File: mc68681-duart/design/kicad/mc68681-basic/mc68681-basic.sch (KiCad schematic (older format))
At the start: 29 parts, among them IC1 68681, IC2 74HCT245, IC3 74HCT245, IC5 74126, IC6 IC6_DECO.PLD, IC7 IC7_UART_.PLD, J1 Conn_02x32_Odd_Even, J2 EXTBUS, J3 UART_A, J4 UART_B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

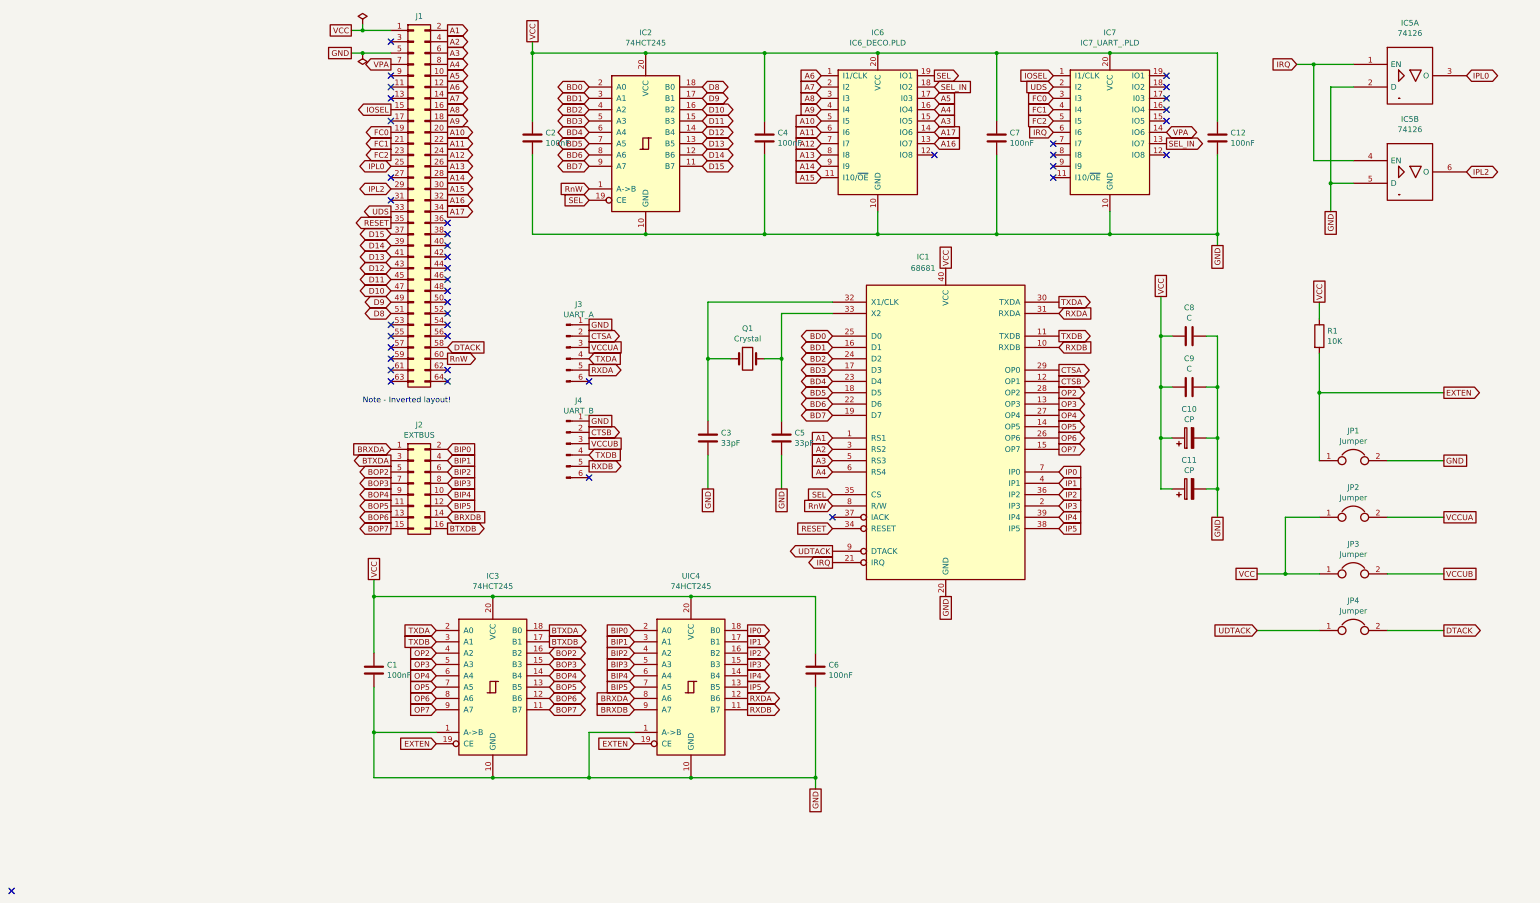
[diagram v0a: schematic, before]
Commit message: r0 layout, PLD changes for same
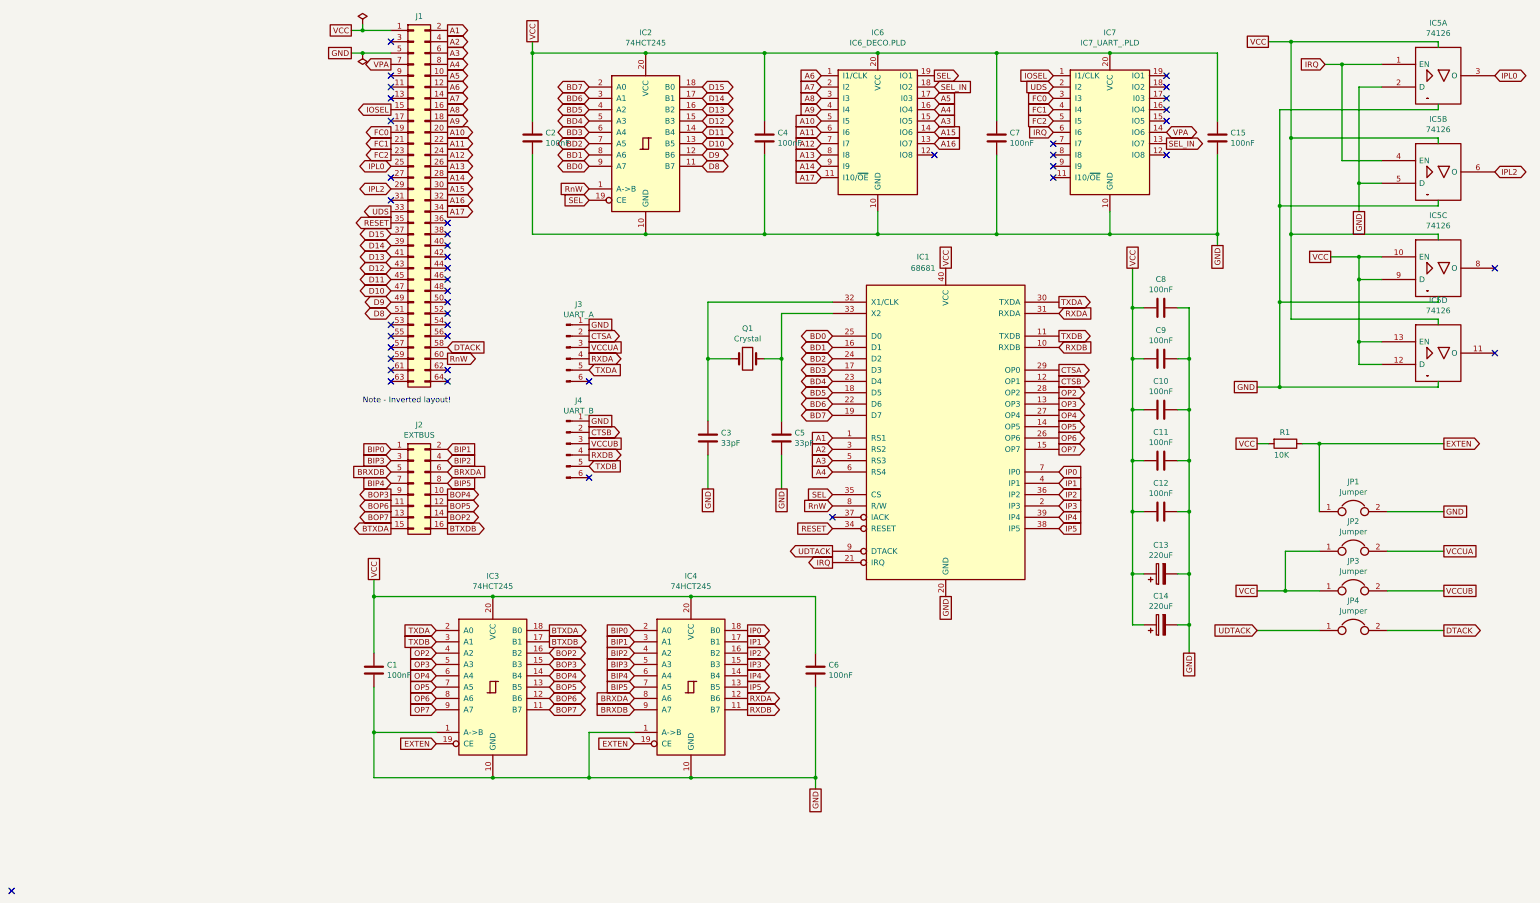
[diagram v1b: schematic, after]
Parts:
- added C10, C11, C12: 100nF, rosco_m68k:C2.5-3, symbol Device:C
- added unit 3 of IC5
- added unit 4 of IC5
- C1, C2, C3, C4, C5, C6, C7: footprint (none) -> rosco_m68k:C2.5-3
- C13: renamed from C10; value CP -> 220uF; footprint (none) -> Capacitor_THT:CP_Radial_D6.3mm_P2.50mm
- C14: renamed from C11; value CP -> 220uF; footprint (none) -> Capacitor_THT:CP_Radial_D6.3mm_P2.50mm
- C15: renamed from C12; footprint (none) -> rosco_m68k:C2.5-3
- C8, C9: value C -> 100nF; footprint (none) -> rosco_m68k:C2.5-3
- IC1: footprint (none) -> Package_DIP:DIP-40_W15.24mm_Socket_LongPads
- IC2, IC3, IC6, IC7: footprint (none) -> Package_DIP:DIP-20_W7.62mm_Socket_LongPads
- IC4: renamed from UIC4; footprint (none) -> Package_DIP:DIP-20_W7.62mm_Socket_LongPads
- IC5: footprint (none) -> Package_DIP:DIP-14_W7.62mm_Socket_LongPads
- J1: footprint rosco_m68k:pin-2X32 -> Connector_PinHeader_2.54mm:PinHeader_2x32_P2.54mm_Vertical
- J2: footprint (none) -> Connector_PinHeader_2.54mm:PinHeader_2x08_P2.54mm_Vertical
- J3, J4: footprint (none) -> Connector_PinHeader_2.54mm:PinHeader_1x06_P2.54mm_Vertical
- JP1, JP2, JP3, JP4: footprint (none) -> Connector_PinHeader_2.54mm:PinHeader_1x02_P2.54mm_Vertical
- Q1: footprint (none) -> Crystal:Crystal_HC49-4H_Vertical
- R1: footprint (none) -> Resistor_THT:R_Axial_DIN0207_L6.3mm_D2.5mm_P10.16mm_Horizontal
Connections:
- net A15: now also IC6.14 (IO6); no longer IC6.11 (I10/~OE~)
- net A17: now also IC6.11 (I10/~OE~); no longer IC6.14 (IO6)
- net BD0: now also IC2.9 (A7); no longer IC2.2 (A0)
- net BD1: now also IC2.8 (A6); no longer IC2.3 (A1)
- net BD2: now also IC2.7 (A5); no longer IC2.4 (A2)
- net BD3: now also IC2.6 (A4); no longer IC2.5 (A3)
- net BD4: now also IC2.5 (A3); no longer IC2.6 (A4)
- net BD5: now also IC2.4 (A2); no longer IC2.7 (A5)
- net BD6: now also IC2.3 (A1); no longer IC2.8 (A6)
- net BD7: now also IC2.2 (A0); no longer IC2.9 (A7)
- net BIP0: now also J2.1 (Pin_1); no longer J2.2 (Pin_2)
- net BIP1: now also J2.2 (Pin_2); no longer J2.4 (Pin_4)
- net BIP2: now also J2.4 (Pin_4); no longer J2.6 (Pin_6)
- net BIP3: now also J2.3 (Pin_3); no longer J2.8 (Pin_8)
- net BIP4: now also J2.7 (Pin_7); no longer J2.10 (Pin_10)
- net BIP5: now also J2.8 (Pin_8); no longer J2.12 (Pin_12)
- net BOP2: now also J2.14 (Pin_14); no longer J2.5 (Pin_5)
- net BOP3: now also J2.9 (Pin_9); no longer J2.7 (Pin_7)
- net BOP4: now also J2.10 (Pin_10); no longer J2.9 (Pin_9)
- net BOP5: now also J2.12 (Pin_12); no longer J2.11 (Pin_11)
- net BOP6: now also J2.11 (Pin_11); no longer J2.13 (Pin_13)
- net BOP7: now also J2.13 (Pin_13); no longer J2.15 (Pin_15)
- net BRXDA: now also J2.6 (Pin_6); no longer J2.1 (Pin_1)
- net BRXDB: now also J2.5 (Pin_5); no longer J2.14 (Pin_14)
- net BTXDA: now also J2.15 (Pin_15); no longer J2.3 (Pin_3)
- net D10: now also IC2.13 (B5); no longer IC2.16 (B2)
- net D11: now also IC2.14 (B4); no longer IC2.15 (B3)
- net D12: now also IC2.15 (B3); no longer IC2.14 (B4)
- net D13: now also IC2.16 (B2); no longer IC2.13 (B5)
- net D14: now also IC2.17 (B1); no longer IC2.12 (B6)
- net D15: now also IC2.18 (B0); no longer IC2.11 (B7)
- net D8: now also IC2.11 (B7); no longer IC2.18 (B0)
- net D9: now also IC2.12 (B6); no longer IC2.17 (B1)
- net EXTEN: now also R1.1; no longer R1.2
- net GND: now also C10.1, C11.1, C12.1, IC5.7 (GND), IC5.7 (GND)
- net RXDA: now also J3.4 (Pin_4); no longer J3.5 (Pin_5)
- net RXDB: now also J4.4 (Pin_4); no longer J4.5 (Pin_5)
- net TXDA: now also J3.5 (Pin_5); no longer J3.4 (Pin_4)
- net TXDB: now also J4.5 (Pin_5); no longer J4.4 (Pin_4)
- net VCC: now also R1.2, C10.2, C11.2, C12.2, IC5.10 (EN), IC5.12 (D), IC5.13 (EN), IC5.14 (VCC), IC5.14 (VCC), IC5.9 (D); no longer R1.1
- no-connect marks 41 -> 43
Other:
- moved on the sheet: C13, C14, C8, C9, IC5A, IC5B, JP1, JP2, JP3, R1

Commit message: Fix a couple of issues...
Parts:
- added R2: 10K, Resistor_THT:R_Axial_DIN0207_L6.3mm_D2.5mm_P10.16mm_Horizontal, symbol Device:R
- IC5: value 74126 -> 74125
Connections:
- net IRQ: now also R2.2
- net VCC: now also R2.1
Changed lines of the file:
@@
 P 10300 1100
 F 0 "IC5" H 10300 1566 50  0000 C CNN
-F 1 "74126" H 10300 1475 50  0000 C CNN
+F 1 "74125" H 10300 1475 50  0000 C CNN
 F 2 "Package_DIP:DIP-14_W7.62mm_Socket_LongPads" H 10300 1100 50  0001 C CNN
 F 3 "" H 10300 1100 50  0001 C CNN
@@
 P 10300 1950
 F 0 "IC5" H 10300 2416 50  0000 C CNN
-F 1 "74126" H 10300 2325 50  0000 C CNN
+F 1 "74125" H 10300 2325 50  0000 C CNN
 F 2 "Package_DIP:DIP-14_W7.62mm_Socket_LongPads" H 10300 1950 50  0001 C CNN
 F 3 "" H 10300 1950 50  0001 C CNN
@@
 Text GLabel 6900 1600 0    50   Input ~ 0
 IRQ
-Text GLabel 4950 5400 0    50   Output ~ 0
+Text GLabel 3700 5400 0    50   Output ~ 0
 IRQ
 Text GLabel 7900 1700 2    50   Output ~ 0
@@
 P 10300 2800
 F 0 "IC5" H 10300 3266 50  0000 C CNN
-F 1 "74126" H 10300 3175 50  0000 C CNN
+F 1 "74125" H 10300 3175 50  0000 C CNN
 F 2 "Package_DIP:DIP-14_W7.62mm_Socket_LongPads" H 10300 2800 50  0001 C CNN
 F 3 "" H 10300 2800 50  0001 C CNN
@@
 P 10300 3550
 F 0 "IC5" H 10300 4016 50  0000 C CNN
-F 1 "74126" H 10300 3925 50  0000 C CNN
+F 1 "74125" H 10300 3925 50  0000 C CNN
 F 2 "Package_DIP:DIP-14_W7.62mm_Socket_LongPads" H 10300 3550 50  0001 C CNN
 F 3 "" H 10300 3550 50  0001 C CNN
@@
 Text GLabel 8700 3850 0    50   UnSpc ~ 0
 GND
+$Comp
+L Device:R R2
+U 1 1 5EFEF14E
+P 4150 5150
+F 0 "R2" H 4220 5196 50  0000 L CNN
+F 1 "10K" H 4220 5105 50  0000 L CNN
+F 2 "Resistor_THT:R_Axial_DIN0207_L6.3mm_D2.5mm_P10.16mm_Horizontal" V 4080 5150 50  0001 C CNN
+F 3 "~" H 4150 5150 50  0001 C CNN
+	1    4150 5150
+	1    0    0    -1
+$EndComp
+Text GLabel 4150 4900 1    50   UnSpc ~ 0
+VCC
+Wire Wire Line
+	3700 5400 4150 5400
+Wire Wire Line
+	4150 4900 4150 5000
+Wire Wire Line
+	4150 5300 4150 5400
+Connection ~ 4150 5400
+Wire Wire Line
+	4150 5400 4950 5400
 $EndSCHEMATC

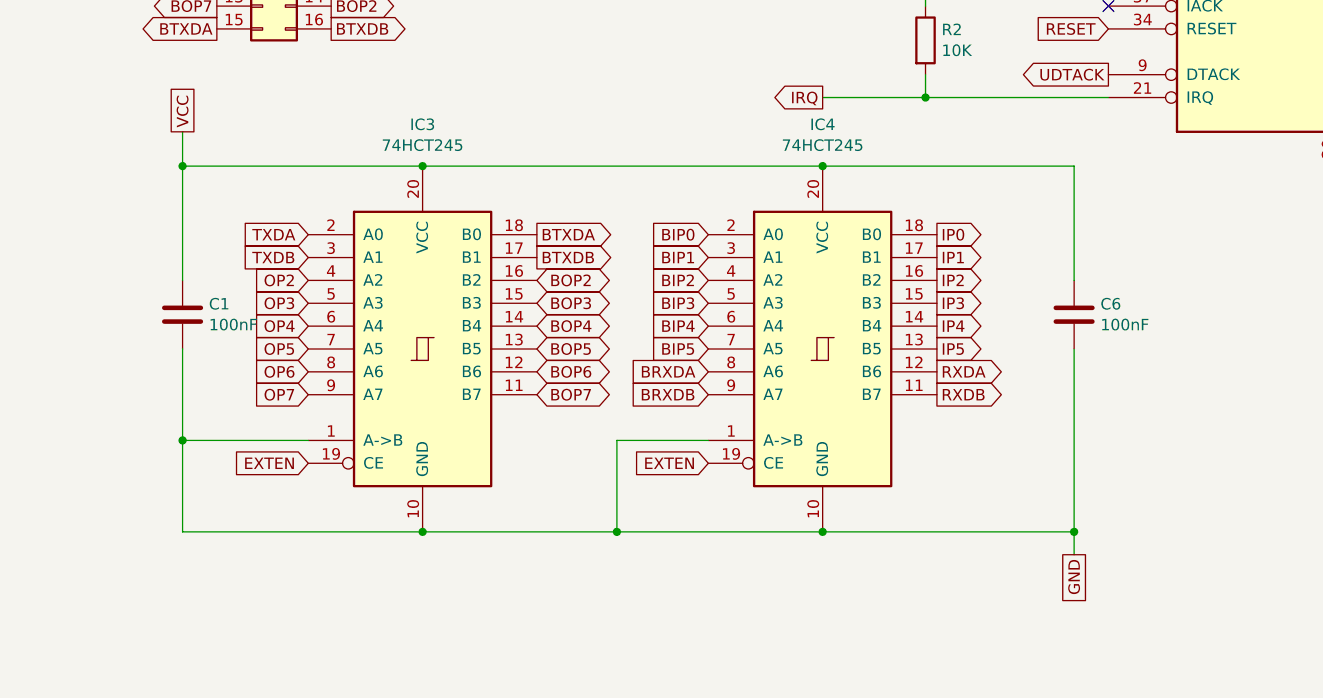
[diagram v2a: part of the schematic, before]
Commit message: Fix incorrect direction for EXT drivers
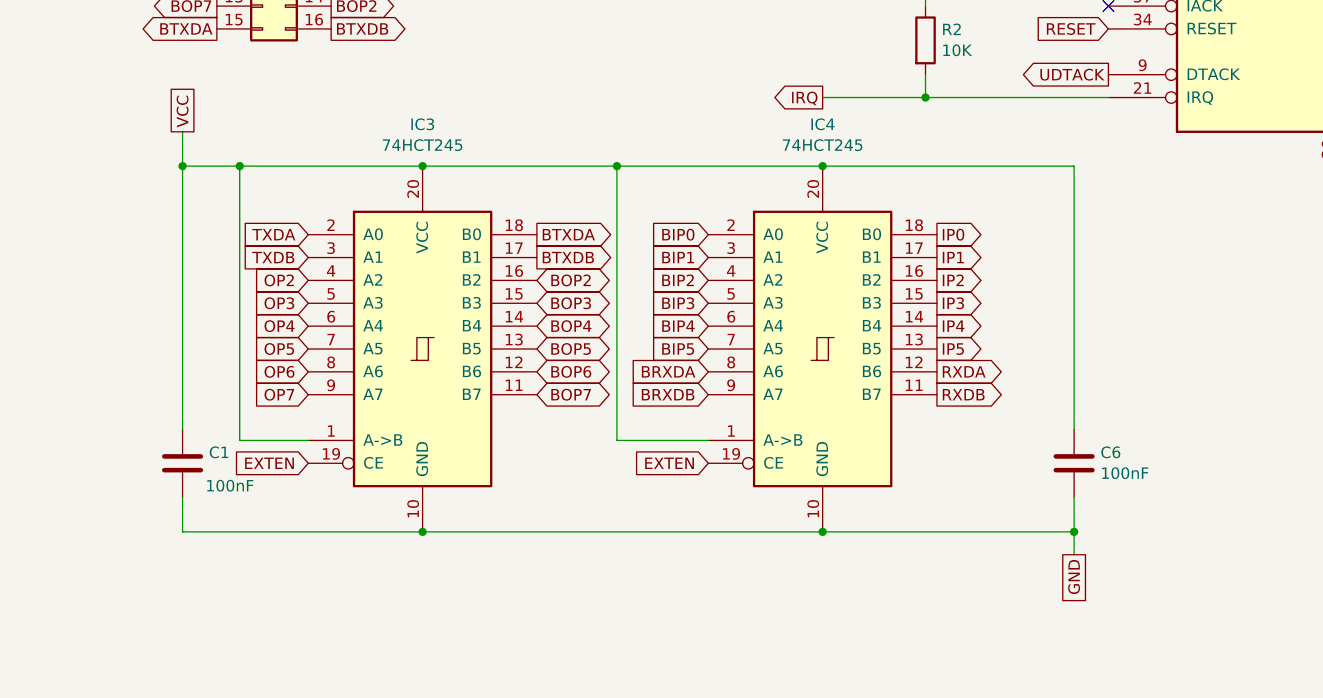
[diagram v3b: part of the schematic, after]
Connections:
- net GND: no longer IC3.1 (A->B), IC4.1 (A->B)
- net VCC: now also IC3.1 (A->B), IC4.1 (A->B)
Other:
- moved on the sheet: C1, C6
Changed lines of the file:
@@
 Wire Wire Line
 	3200 6900 2800 6900
-Wire Wire Line
-	2800 6900 2800 7300
-Wire Wire Line
-	2800 7300 3700 7300
-Wire Wire Line
-	1950 7300 2800 7300
-Connection ~ 2800 7300
 Connection ~ 1950 7300
 Text GLabel 3200 6000 0    50   Input ~ 0
@@
 GND
 $Comp
-L Device:C C1
-U 1 1 5EF75A30
-P 900 6350
-F 0 "C1" H 1015 6396 50  0000 L CNN
-F 1 "100nF" H 1015 6305 50  0000 L CNN
-F 2 "rosco_m68k:C2.5-3" H 938 6200 50  0001 C CNN
-F 3 "~" H 900 6350 50  0001 C CNN
-	1    900  6350
-	1    0    0    -1
-$EndComp
-$Comp
 L Device:C C6
 U 1 1 5EF76323
-P 4800 6350
-F 0 "C6" H 4915 6396 50  0000 L CNN
-F 1 "100nF" H 4915 6305 50  0000 L CNN
-F 2 "rosco_m68k:C2.5-3" H 4838 6200 50  0001 C CNN
-F 3 "~" H 4800 6350 50  0001 C CNN
-	1    4800 6350
-	1    0    0    -1
-$EndComp
-Wire Wire Line
-	900  5700 1950 5700
+P 4800 7000
+F 0 "C6" H 4915 7046 50  0000 L CNN
+F 1 "100nF" H 4915 6955 50  0000 L CNN
+F 2 "rosco_m68k:C2.5-3" H 4838 6850 50  0001 C CNN
+F 3 "~" H 4800 7000 50  0001 C CNN
+	1    4800 7000
+	1    0    0    -1
+$EndComp
+Wire Wire Line
+	900  5700 1150 5700
 Wire Wire Line
 	3700 5700 4800 5700
 Wire Wire Line
-	4800 5700 4800 6200
-Wire Wire Line
-	1950 5700 3700 5700
+	4800 5700 4800 6850
+Wire Wire Line
+	1950 5700 2800 5700
 Connection ~ 1950 5700
 Connection ~ 3700 5700
 Wire Wire Line
-	900  6500 900  6900
-Wire Wire Line
 	900  7300 1950 7300
 Wire Wire Line
-	900  6900 1450 6900
-Connection ~ 900  6900
-Wire Wire Line
-	900  6900 900  7300
-Wire Wire Line
 	3700 7300 4800 7300
 Wire Wire Line
-	4800 7300 4800 6500
+	4800 7300 4800 7150
 Connection ~ 3700 7300
 Wire Wire Line
-	900  5700 900  6200
-Wire Wire Line
 	900  5700 900  5550
-Connection ~ 900  5700
 Wire Wire Line
 	4800 7300 4800 7400
@@
 Wire Wire Line
 	4150 5400 4950 5400
+$Comp
+L Device:C C1
+U 1 1 5EF75A30
+P 900 7000
+F 0 "C1" H 1015 7046 50  0000 L CNN
+F 1 "100nF" H 1000 6900 50  0000 L CNN
+F 2 "rosco_m68k:C2.5-3" H 938 6850 50  0001 C CNN
+F 3 "~" H 900 7000 50  0001 C CNN
+	1    900  7000
+	1    0    0    -1
+$EndComp
+Wire Wire Line
+	900  7150 900  7300
+Connection ~ 900  5700
+Wire Wire Line
+	1450 6900 1150 6900
+Wire Wire Line
+	900  5700 900  6850
+Wire Wire Line
+	1150 5700 1150 6900
+Connection ~ 1150 5700
+Wire Wire Line
+	1150 5700 1950 5700
+Wire Wire Line
+	1950 7300 3700 7300
+Wire Wire Line
+	2800 6900 2800 5700
+Connection ~ 2800 5700
+Wire Wire Line
+	2800 5700 3700 5700
 $EndSCHEMATC

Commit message: Fixes for 1.2 mainboard
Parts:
- C3, C5: value 33pF -> 7pF
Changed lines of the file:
@@
 P 3850 4300
 F 0 "C3" H 3965 4346 50  0000 L CNN
-F 1 "33pF" H 3965 4255 50  0000 L CNN
+F 1 "7pF" H 3965 4255 50  0000 L CNN
 F 2 "rosco_m68k:C2.5-3" H 3888 4150 50  0001 C CNN
 F 3 "~" H 3850 4300 50  0001 C CNN
@@
 P 4500 4300
 F 0 "C5" H 4615 4346 50  0000 L CNN
-F 1 "33pF" H 4615 4255 50  0000 L CNN
+F 1 "7pF" H 4615 4255 50  0000 L CNN
 F 2 "rosco_m68k:C2.5-3" H 4538 4150 50  0001 C CNN
 F 3 "~" H 4500 4300 50  0001 C CNN
